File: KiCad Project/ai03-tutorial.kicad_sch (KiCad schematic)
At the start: 14 parts, among them SW1 SW_Push, U1 ATmega32U4-A, Y1 16MHz

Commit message: Finished PCB guide part 4 - schematic.
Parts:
- added D1, D2, D3, D4: D_Small, Diode_SMD:D_SOD-123, symbol Device:D_Small
- added F1: Polyfuse, Fuse:Fuse_1206_3216Metric, symbol Device:Polyfuse
- added MX1, MX2, MX3, MX4: MX-NoLED, MX_Alps_Hybrid:MX-1U-NoLED, symbol MX_Alps_Hybrid:MX-NoLED
- added USB1: Molex-0548190589, random-keyboard-parts:Molex-0548190589, symbol random-keyboard-parts:Molex-0548190589
- C1, C2, C3, C4, C5, C6, C7: footprint (none) -> Capacitor_SMD:C_0805_2012Metric
- R1, R2, R3, R4: footprint (none) -> Resistor_SMD:R_0805_2012Metric
- SW1: footprint (none) -> random-keyboard-parts:SKQG-1155865
- Y1: footprint (none) -> Crystal:Crystal_SMD_3225-4Pin_3.2x2.5mm
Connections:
- net +5V: now also F1.2
- net D+: now also USB1.3 (D+)
- net D-: now also USB1.4 (D-)
- net GND: now also USB1.1 (GND)
- new net: D1.2 (A), MX1.2 (ROW)
- new net: D3.2 (A), MX3.2 (ROW)
- new net: D4.2 (A), MX4.2 (ROW)
- new net: D2.2 (A), MX2.2 (ROW)
- new net COL0: MX1.1 (COL), MX3.1 (COL)
- new net COL1: MX2.1 (COL), MX4.1 (COL)
- new net ROW0: D1.1 (K), D2.1 (K)
- new net ROW1: D3.1 (K), D4.1 (K)
- new net VCC: F1.1, USB1.6 (SHIELD)
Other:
- moved on the sheet: C2, C3, C4, C5

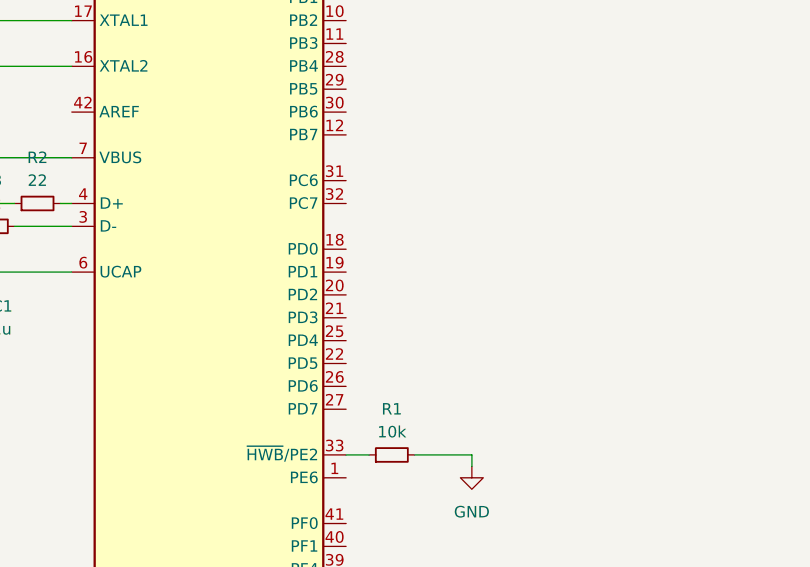
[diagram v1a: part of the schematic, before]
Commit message: Added matrix connections.
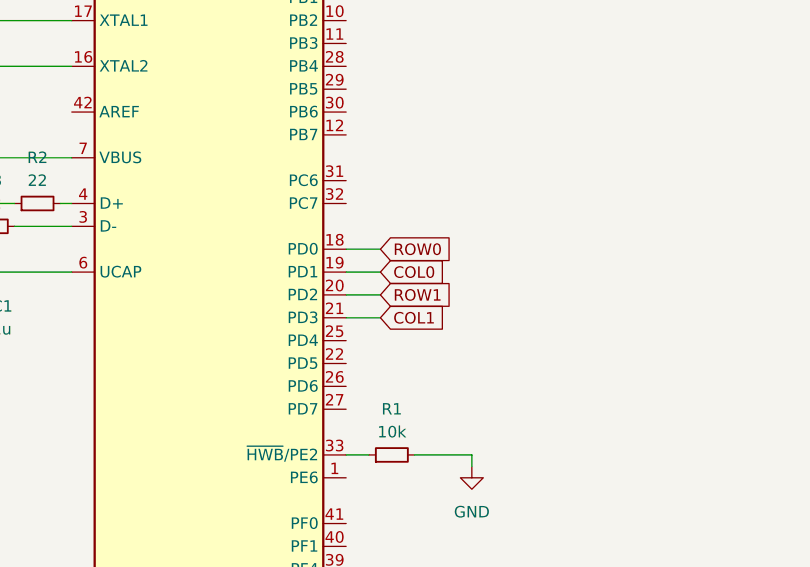
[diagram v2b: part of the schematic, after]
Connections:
- net COL0: now also U1.19 (PD1)
- net COL1: now also U1.21 (PD3)
- net ROW0: now also U1.18 (PD0)
- net ROW1: now also U1.20 (PD2)
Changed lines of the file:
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@@
+    (stroke (width 0) (type default))
+  )
+  (wire (pts (xy 184.15 86.36) (xy 180.34 86.36))
     (stroke (width 0) (type default))
   )
@@
     (stroke (width 0) (type default))
   )
+  (wire (pts (xy 184.15 91.44) (xy 180.34 91.44))
+    (stroke (width 0) (type default))
+  )
   (wire (pts (xy 113.03 63.5) (xy 111.76 63.5))
     (stroke (width 0) (type default))
@@
     (stroke (width 0) (type default))
   )
+  (wire (pts (xy 184.15 88.9) (xy 180.34 88.9))
+    (stroke (width 0) (type default))
+  )
   (wire (pts (xy 132.08 55.88) (xy 133.35 55.88))
     (stroke (width 0) (type default))
@@
     (stroke (width 0) (type default))
   )
+  (wire (pts (xy 184.15 93.98) (xy 180.34 93.98))
+    (stroke (width 0) (type default))
+  )
   (wire (pts (xy 247.65 78.74) (xy 247.65 80.01))
     (stroke (width 0) (type default))
@@
   (wire (pts (xy 240.03 120.65) (xy 240.03 119.38))
     (stroke (width 0) (type default))
+  )
+  (global_label "COL0" (shape input) (at 184.15 88.9 0) (fields_autoplaced)
+    (effects (font (size 1.27 1.27)) (justify left))
+    (property "Intersheetrefs" "${INTERSHEET_REFS}" (at 191.9733 88.9 0)
+      (effects (font (size 1.27 1.27)) (justify left) hide)
+    )
   )
   (global_label "D+" (shape input) (at 137.16 81.28 180) (fields_autoplaced)
@@
     )
   )
+  (global_label "COL1" (shape input) (at 184.15 93.98 0) (fields_autoplaced)
+    (effects (font (size 1.27 1.27)) (justify left))
+    (property "Intersheetrefs" "${INTERSHEET_REFS}" (at 191.9733 93.98 0)
+      (effects (font (size 1.27 1.27)) (justify left) hide)
+    )
+  )
   (global_label "D-" (shape input) (at 254 34.29 0) (fields_autoplaced)
     (effects (font (size 1.27 1.27)) (justify left))
@@
     (effects (font (size 1.27 1.27)) (justify left))
     (property "Intersheetrefs" "${INTERSHEET_REFS}" (at 274.32 55.6767 90)
+      (effects (font (size 1.27 1.27)) (justify left) hide)
+    )
+  )
+  (global_label "ROW1" (shape input) (at 184.15 91.44 0) (fields_autoplaced)
+    (effects (font (size 1.27 1.27)) (justify left))
+    (property "Intersheetrefs" "${INTERSHEET_REFS}" (at 192.3966 91.44 0)
       (effects (font (size 1.27 1.27)) (justify left) hide)
     )
@@
     )
   )
+  (global_label "ROW0" (shape input) (at 184.15 86.36 0) (fields_autoplaced)
+    (effects (font (size 1.27 1.27)) (justify left))
+    (property "Intersheetrefs" "${INTERSHEET_REFS}" (at 192.3966 86.36 0)
+      (effects (font (size 1.27 1.27)) (justify left) hide)
+    )
+  )
